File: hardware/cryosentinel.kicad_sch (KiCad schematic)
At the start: 42 parts, among them J1 USB-C-16P, J2 JST-PH-2, J3 U.FL LoRa Antenna, J4 U.FL GPS Antenna, Q1 MMBT2222, U1 ESP32-C3-MINI-1, U10 1.54in e-ink FPC-8, U11 AT25DF321, U2 SHT40, U3 ATECC608A, U4 ST25DV04K, U5 ADXL345, U6 SX1262, U7 MAX-M10S, U8 MAX17048, U9 TP4056

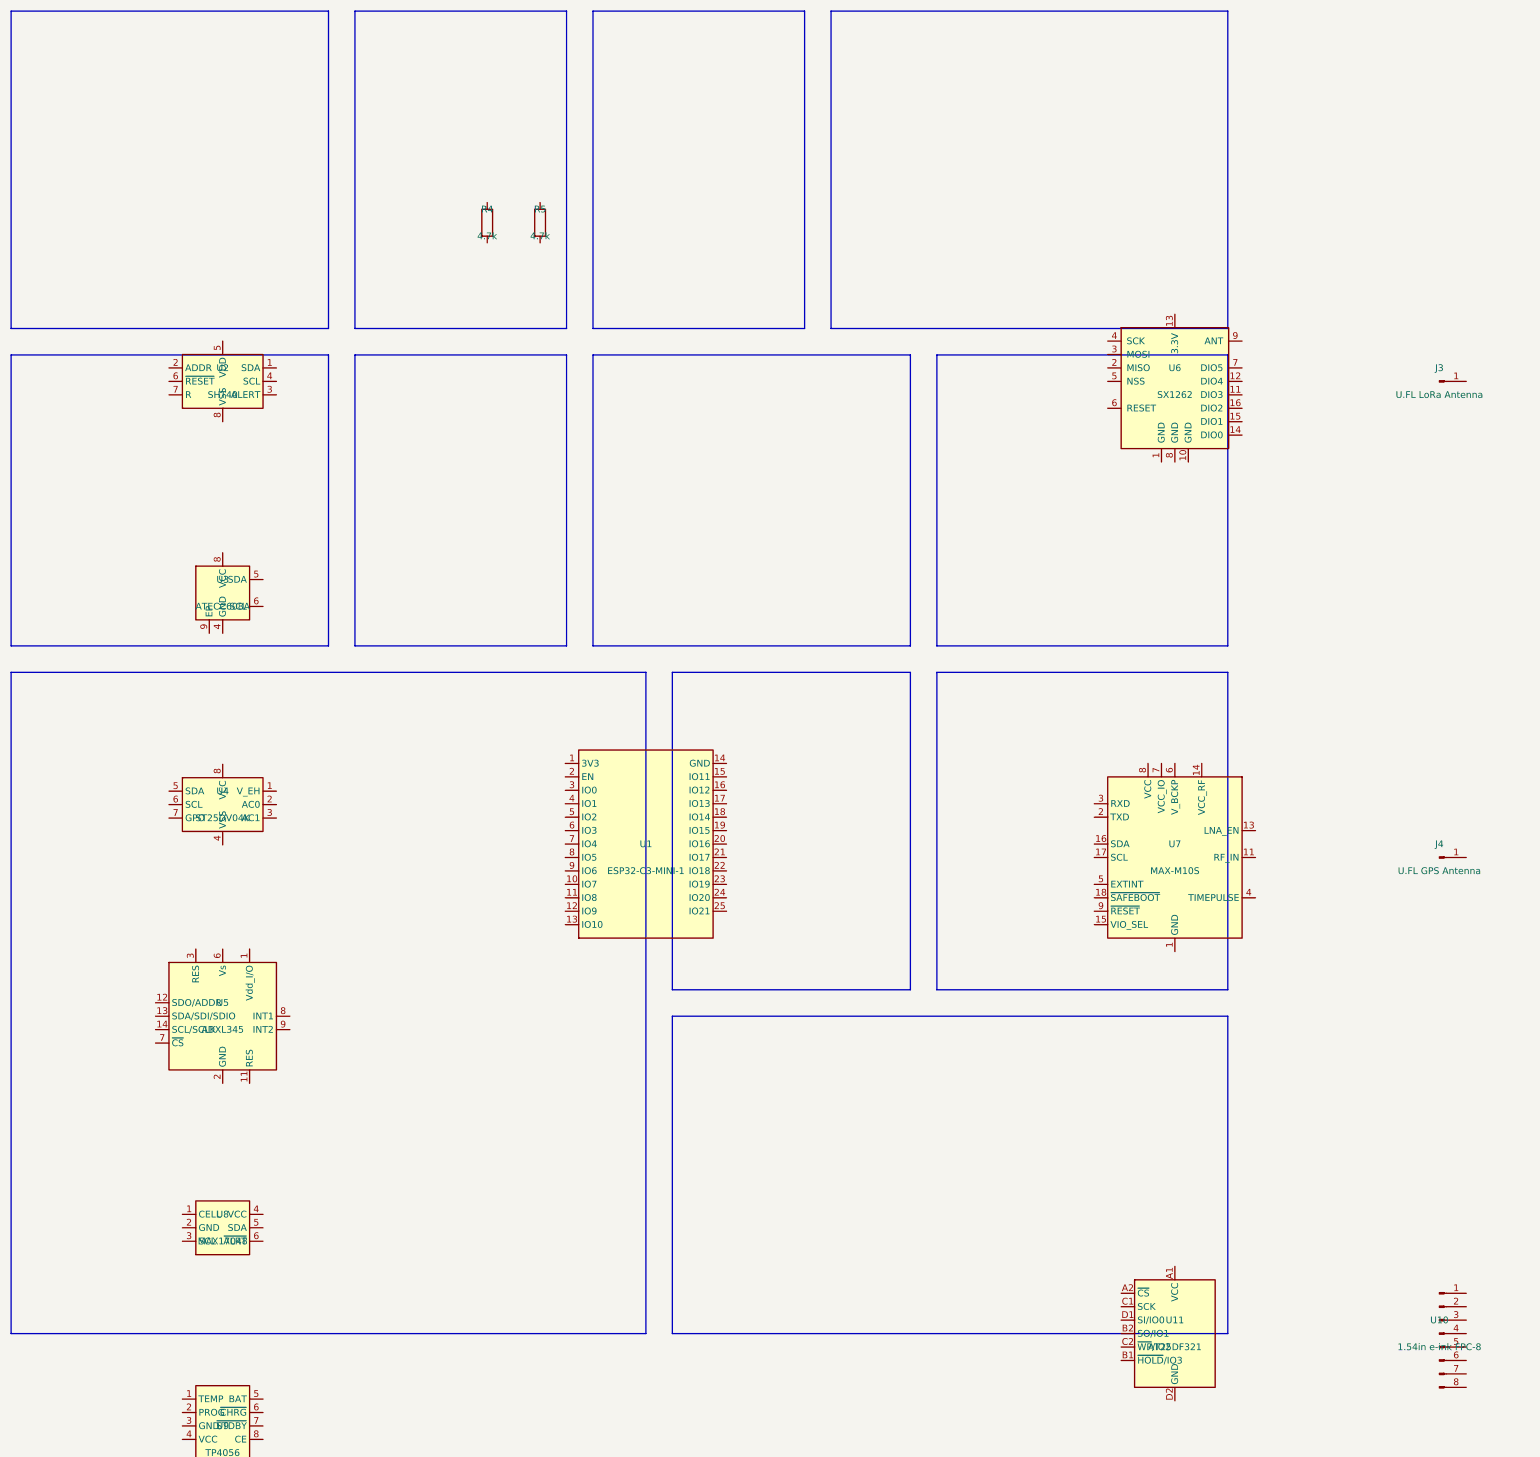
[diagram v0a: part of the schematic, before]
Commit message: fix: Restore original modular schematic layout, fix Mermaid parsing errors by removing emojis and unsupported links
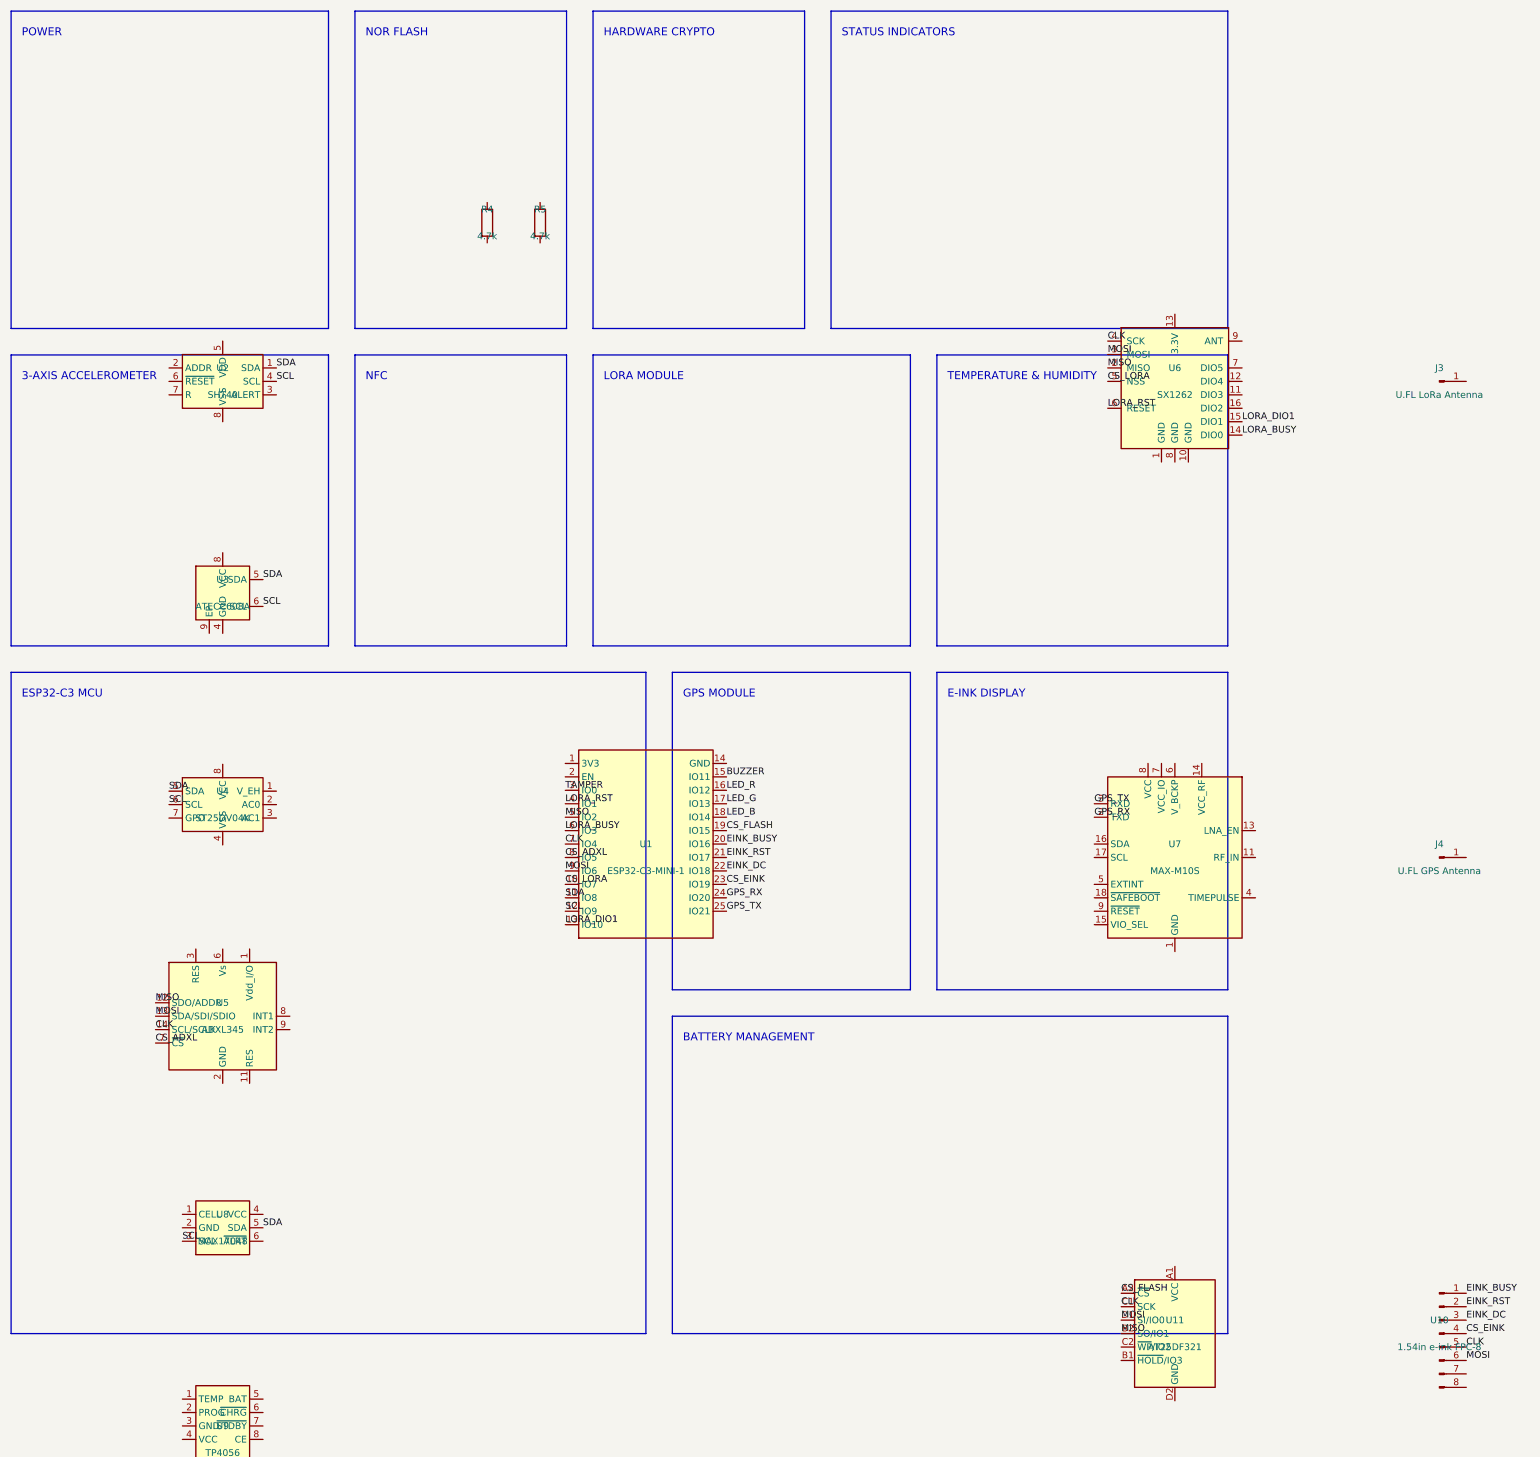
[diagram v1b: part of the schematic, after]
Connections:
- net SCL: now reaches U8.3 (SCL)
- net SCL: now also U1.12 (IO9), U2.4 (SCL), U3.6 (SCL), U4.6 (SCL)
- net SDA: now reaches U8.5 (SDA)
- net SDA: now also U1.11 (IO8), U2.1 (SDA), U3.5 (SDA), U4.5 (SDA)
- net CS_LORA: now reaches U1.10 (IO7)
- net CS_LORA: now also U6.5 (NSS)
- net LORA_DIO1: now reaches U1.13 (IO10)
- net LORA_DIO1: now also U6.15 (DIO1)
- net BUZZER: now reaches U1.15 (IO11)
- net LED_R: now reaches U1.16 (IO12)
- net LED_G: now reaches U1.17 (IO13)
- net LED_B: now reaches U1.18 (IO14)
- net CS_FLASH: now reaches U1.19 (IO15)
- net CS_FLASH: now also U11.A2 (~{CS})
- net EINK_BUSY: now reaches U1.20 (IO16)
- net EINK_BUSY: now also U10.1 (Pin_1)
- net EINK_RST: now reaches U1.21 (IO17)
- net EINK_RST: now also U10.2 (Pin_2)
- net EINK_DC: now reaches U1.22 (IO18)
- net EINK_DC: now also U10.3 (Pin_3)
- net CS_EINK: now reaches U1.23 (IO19)
- net CS_EINK: now also U10.4 (Pin_4)
- net GPS_RX: now reaches U1.24 (IO20)
- net GPS_RX: now also U7.2 (TXD)
- net GPS_TX: now reaches U1.25 (IO21)
- net GPS_TX: now also U7.3 (RXD)
- net TAMPER: now reaches U1.3 (IO0)
- net LORA_RST: now reaches U1.4 (IO1)
- net LORA_RST: now also U6.6 (RESET)
- net MISO: now reaches U1.5 (IO2)
- net MISO: now also U11.B2 (SO/IO1), U5.12 (SDO/ADDR), U6.2 (MISO)
- net LORA_BUSY: now reaches U1.6 (IO3)
- net LORA_BUSY: now also U6.14 (DIO0)
- net CLK: now reaches U1.7 (IO4)
- net CLK: now also U10.5 (Pin_5), U11.C1 (SCK), U5.14 (SCL/SCLK), U6.4 (SCK)
- net CS_ADXL: now reaches U1.8 (IO5)
- net CS_ADXL: now also U5.7 (~{CS})
- net MOSI: now reaches U1.9 (IO6)
- net MOSI: now also U10.6 (Pin_6), U11.D1 (SI/IO0), U5.13 (SDA/SDI/SDIO), U6.3 (MOSI)
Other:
- note added: "3-AXIS ACCELEROMETER"
- note added: "BATTERY MANAGEMENT"
- note added: "E-INK DISPLAY"
- note added: "ESP32-C3 MCU"
- note added: "GPS MODULE"
- note added: "HARDWARE CRYPTO"
- note added: "LORA MODULE"
- note added: "NFC"
- note added: "NOR FLASH"
- note added: "POWER"
- note added: "STATUS INDICATORS"
- note added: "TEMPERATURE & HUMIDITY"
